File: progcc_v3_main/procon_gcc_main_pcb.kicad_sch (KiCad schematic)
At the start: 104 parts, among them J1 Rumble, J2 Rumble, J3 To Button Board, J4 Conn_01x06_Female, J5 Conn_01x02_Pin, J9 USB_C_Receptacle, Q1 Q_PMOS_GDS, Q2 Q_NMOS_GSD, Q3 Q_NMOS_GSD, Q4 BSS138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

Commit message: Major updates
-Revised button board outline
-Added IMU for motion
-Cleaned up traces on main board
-Add test pads to button board
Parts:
- removed JP1, JP2: SolderJumper_2_Open, Jumper:SolderJumper-2_P1.3mm_Open_TrianglePad1.0x1.5mm, symbol Jumper:SolderJumper_2_Open
- removed R21: 33, Resistor_SMD:R_0402_1005Metric_Pad0.72x0.64mm_HandSolder, symbol Device:R
- removed R23, R24: 0, Resistor_SMD:R_0402_1005Metric, symbol Device:R
- removed U5: GL16112, progcc_v3:MSOP10, symbol progcc_v3:GL16112
- added C14: 100nF, Capacitor_SMD:C_0603_1608Metric, symbol Device:C
- added P1: Endpoint, Connector_PinHeader_2.54mm:PinHeader_1x01_P2.54mm_Vertical, symbol Connector_Generic:Conn_01x01
- added R21: 10k, Resistor_SMD:R_0402_1005Metric, symbol Device:R_Small
- added TP10, TP12, TP15, TP16: TestPoint, TestPoint:TestPoint_Pad_D1.5mm, symbol Connector:TestPoint
- added U11, U5: ST_LSM6, progcc_v3:LGA14, symbol progcc_v3:ST_LSM6
- C5, C6: value 4.7uF -> 100nF; footprint Capacitor_SMD:C_0402_1005Metric -> Capacitor_SMD:C_0603_1608Metric; Group (none) -> C_100nF; LCSC C15849 -> C1525
- C7: value 0.1uF -> 100nF; footprint Capacitor_SMD:C_0402_1005Metric -> Capacitor_SMD:C_0603_1608Metric; Group (none) -> C_100nF; LCSC C15849 -> C1525
- D2, D3, D4: MPN (none) -> CUS08F30
- J1, J2: symbol Connector:Conn_01x02_Male -> progcc_v3:Conn_01x02_Male; now not fitted; now left out of the parts list
- J3: footprint procon_gcc:molex_5051101492_14P -> progcc_v3:molex_5051101492_14P; MPN (none) -> molex_5051101492_14P
- J4, J5, T1, T2, T3, T4, TP6: now not fitted; now left out of the parts list
- J9: MPN (none) -> Shou Han Type-C 24P QCHT
- L1, L2, L3, L4, L5, L6, L7, L8: MPN (none) -> SK6805-EC-15
- Q4, Q5, Q6: MPN (none) -> BSS138
- R20: value 0 -> 500K; Group (none) -> R_500K; LCSC (none) -> C11616
- SW1, SW2: MPN (none) -> GL18
- SW3: MPN (none) -> TS-1187A-B-A-B
- SW4: value ~ -> TS35CA; MPN (none) -> TS35CA
- U1, U2, U3, U4: MPN (none) -> GH39F
- U10, U8: MPN (none) -> MCP3002
- U6: MPN (none) -> RP2040
- U7: MPN (none) -> LP3986-33B3F
- U9: MPN (none) -> W25Q128JVS
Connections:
- net P_LCS is gone; now on net LADC_CS: U8.1 (~{CS}/SHDN)
- net +3V3: now also C5.2, C6.2, C7.2, C14.2, R21.1, U11.5 (VDDIO), U11.8 (VDD), U5.5 (VDDIO), U5.8 (VDD); no longer C6.1, C7.1, R20.1
- net D+: now also TP12.1
- net D-: now also TP10.1
- net GND: now also C5.1, C6.1, C7.1, C14.1, U11.2 (SDx), U11.3 (SCx), U11.6 (GNDIO), U11.7 (GND), U5.2 (SDx), U5.3 (SCx), U5.6 (GNDIO), U5.7 (GND); no longer C5.2, C6.2, C7.2
- net RUN: now also R21.2
- net TOUCH_IN: now reaches U6.38 (GPIO26_ADC0)
- net TOUCH_IN: now also R20.1
- net TOUCH_OUT: now reaches U6.39 (GPIO27_ADC1)
- net TOUCH_OUT: now also R20.2, P1.1 (Pin_1)
- net IMU0_CS: now reaches U6.40 (GPIO28_ADC2)
- net IMU0_CS: now also U5.12 (CS)
- net IMU1_CS: now reaches U6.41 (GPIO29_ADC3)
- net IMU1_CS: now also U11.12 (CS)
- net GPIO1 renamed LADC_CS
- net GULI_CALIBRATE renamed GP1
- net GP1: now also TP15.1; no longer C5.1
- net GULI_DZONE renamed GP2
- net GP2: now also TP16.1
- net P_CLK renamed SPI_CK
- net SPI_CK: now also U11.13 (SCL), U5.13 (SCL)
- net P_RCS renamed RADC_CS
- net P_RX renamed SPI_TX
- net SPI_TX: now also U11.14 (SDA), U5.14 (SDA)
- net P_TX renamed SPI_RX
- net SPI_RX: now also U11.1 (SDO), U5.1 (SDO)
- no-connect marks 0 -> 8
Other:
- note added: "ADCs"
- note added: "CAPACITIVE"
- note added: "Extra GPIO"
- note added: "IMU 0"
- note added: "IMU 1"
- note removed: "Alternate ADC Selection"
- note removed: "Alternate ADCs"
- note removed: "GL Calibrate Enable"
- note removed: "GL Deadzone Enable"
- note removed: "GuliKit ADC IC"
- moved on the sheet: C1, C11, C12, R14, SW3, U9

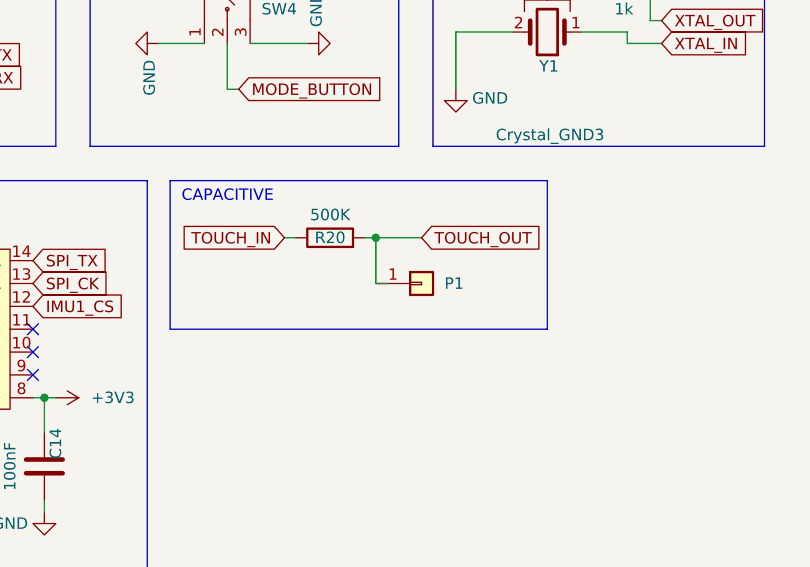
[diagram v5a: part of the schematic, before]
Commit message: Fix Stick positions (More!)
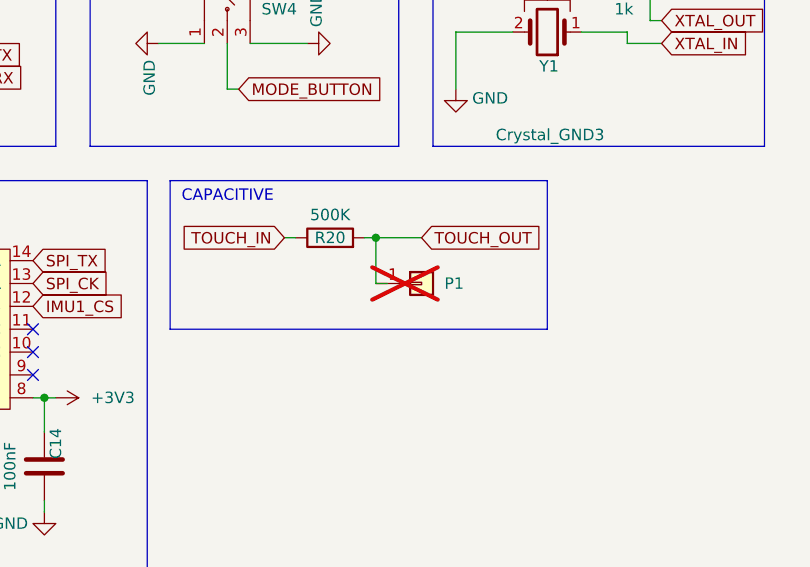
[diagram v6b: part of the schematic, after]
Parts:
- P1: now not fitted; now left out of the parts list
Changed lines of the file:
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@@
   )
   (symbol (lib_id "Connector_Generic:Conn_01x01") (at 246.38 200.66 0) (unit 1)
-    (in_bom yes) (on_board yes) (dnp no)
+    (in_bom no) (on_board yes) (dnp yes)
     (property "Reference" "P1" (at 248.92 200.66 0)
       (effects (font (size 1.27 1.27)) (justify left))
